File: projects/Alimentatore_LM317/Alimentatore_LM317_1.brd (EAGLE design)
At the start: 65.4 x 99.4 mm, 19 parts

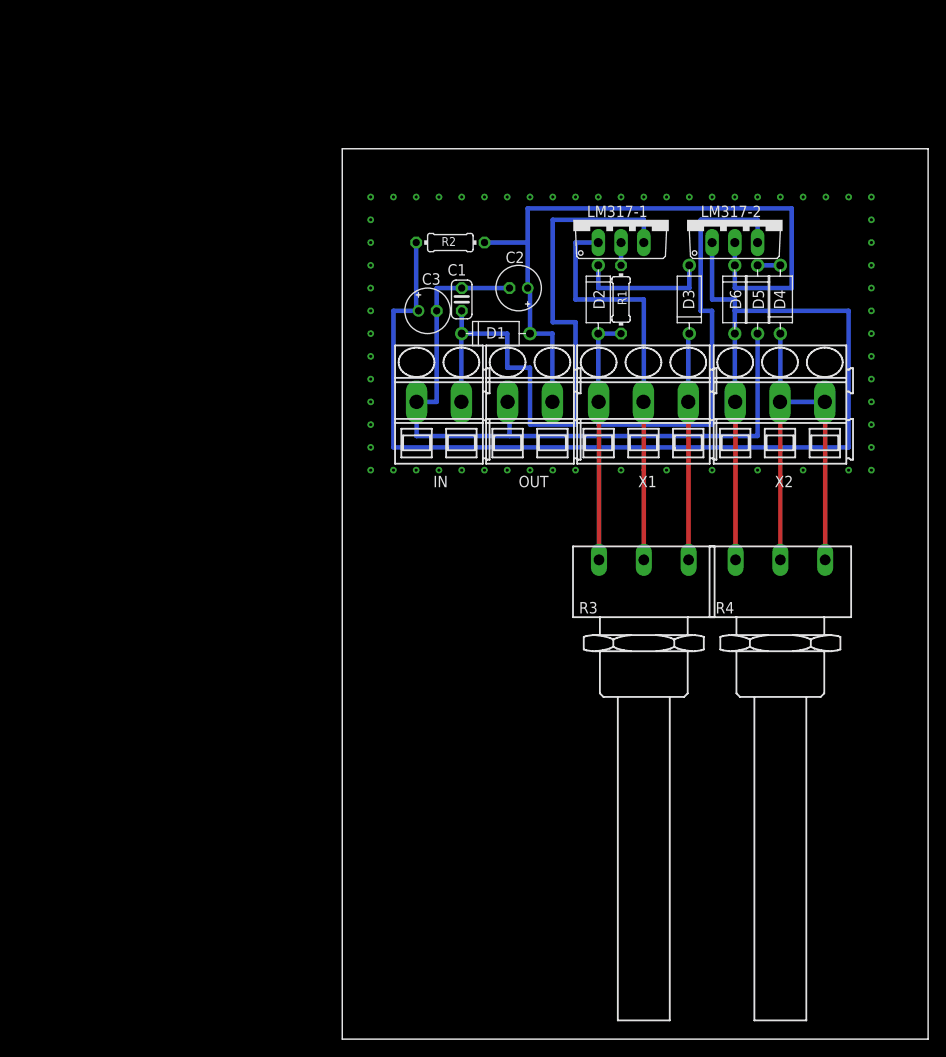
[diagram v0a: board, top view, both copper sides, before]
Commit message: creata seconda versione della scheda. esportate immagini.
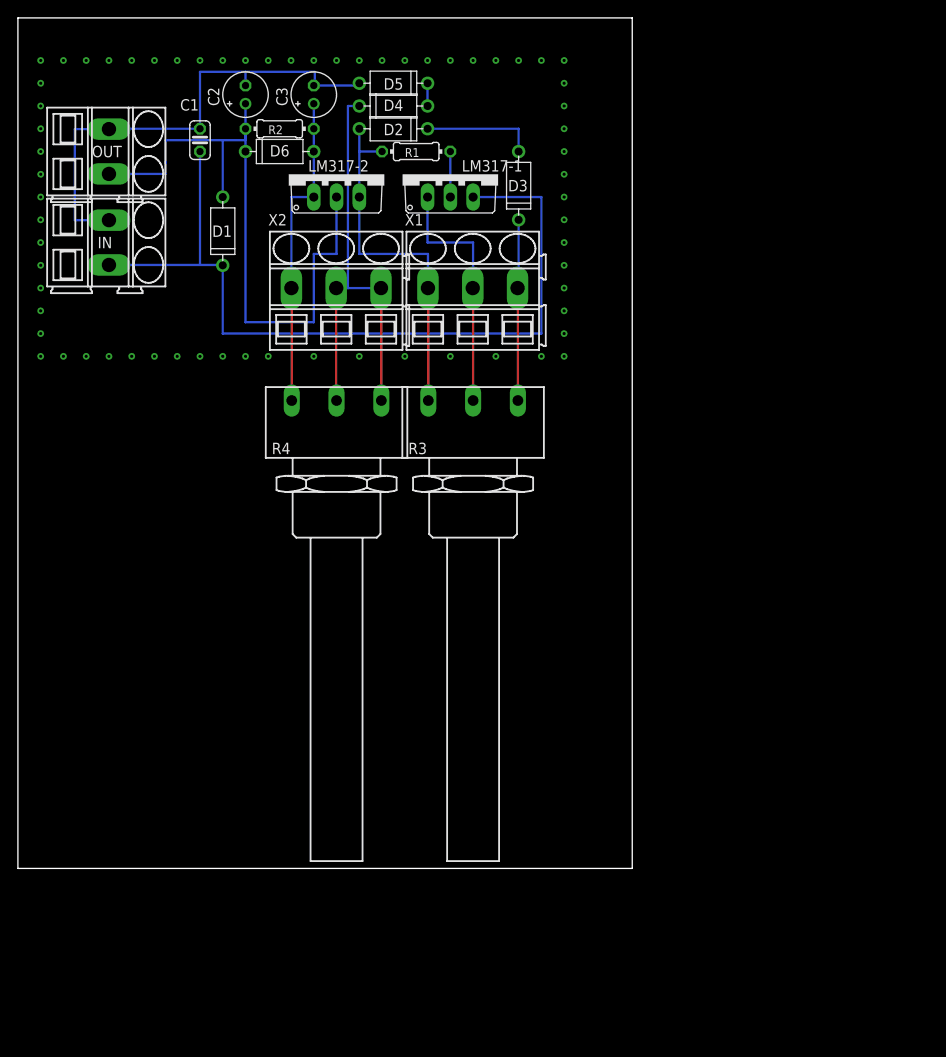
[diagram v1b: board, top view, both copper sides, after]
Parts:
- X1, X2: value (none) -> SMKDSP_1,5/3
- moved OUT 54.7 mm to (10.2, 77.5), turned to 270 degrees
- moved D6 53.4 mm to (29.2, 77.5), turned to 0 degrees
- moved R4 52.6 mm to (35.6, 43.2)
- moved X2 51.1 mm to (33.0, 62.2)
- moved D4 48.3 mm to (41.9, 82.5), turned to 0 degrees
- moved D5 47.3 mm to (41.9, 85.1), turned to 180 degrees
- moved LM317-2 44.7 mm to (35.6, 74.9)
- moved IN 40.9 mm to (10.2, 67.3), turned to 270 degrees
- moved C2 37.4 mm to (25.4, 83.8), turned to 90 degrees
- moved C1 34.2 mm to (20.3, 78.7)
- moved D1 32.6 mm to (22.9, 68.6), turned to 90 degrees
- moved D2 29.8 mm to (41.9, 80.0), turned to 180 degrees
- moved R1 28.2 mm to (44.5, 77.5), turned to 0 degrees
- moved C3 27.3 mm to (33.0, 83.8), turned to 90 degrees
- moved R3 26.1 mm to (50.8, 43.2)
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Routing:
- net N$9: track 142.7 -> 35.7 mm
- net N$3: track 76.1 -> 40.5 mm
- net GND: track 80.5 -> 55.5 mm
- net VCC: track 71.2 -> 91.5 mm
- net N$5: track 45.6 -> 27.9 mm
- net N$7: track 25.4 -> 20.3 mm
- net N$10: track 48.0 -> 51.8 mm, vias 1 -> 0
- net N$1: track 79.0 -> 75.2 mm
- net N$4: track 15.2 -> 12.7 mm
- net N$2: track 2.54 -> 5.08 mm
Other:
- board size 65.4 x 99.4 mm -> 68.6 x 94.9 mm
